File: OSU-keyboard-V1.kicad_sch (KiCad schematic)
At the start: 21 parts, among them J1 AVR-ISP-6, SW1 SW_Push_Dual, U1 ATmega32U4-A, U2 PRTR5V0U2X, Y1 16MHz

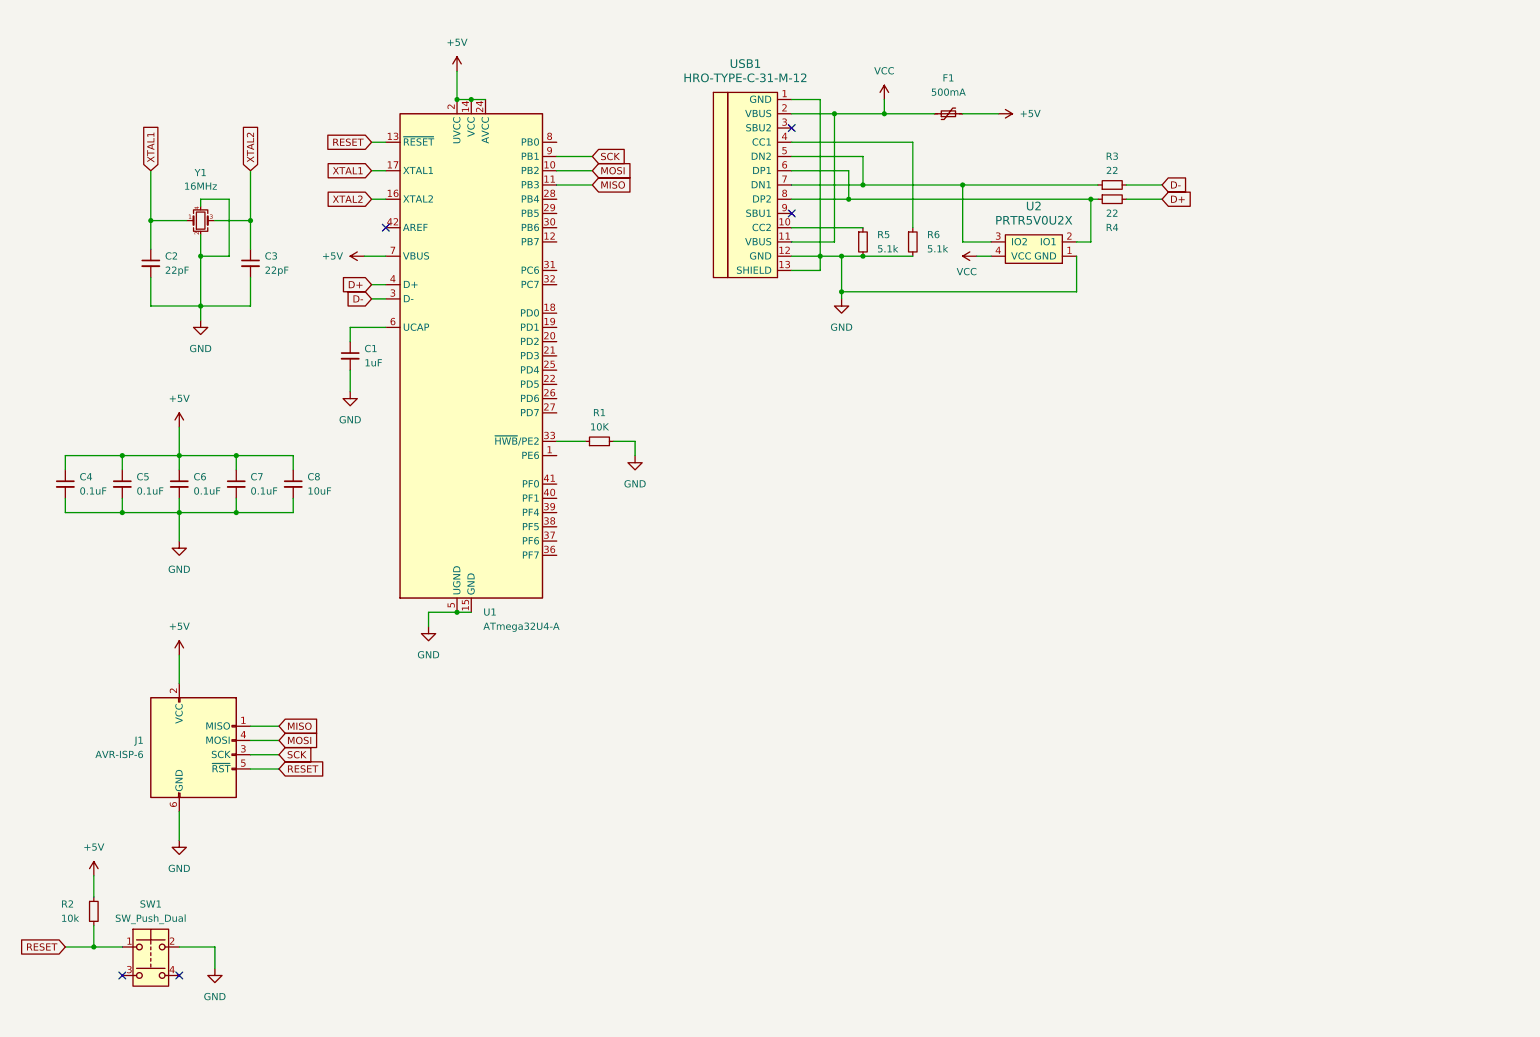
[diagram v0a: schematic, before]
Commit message: Placing components in PCB
Placing all of them (for the first time)
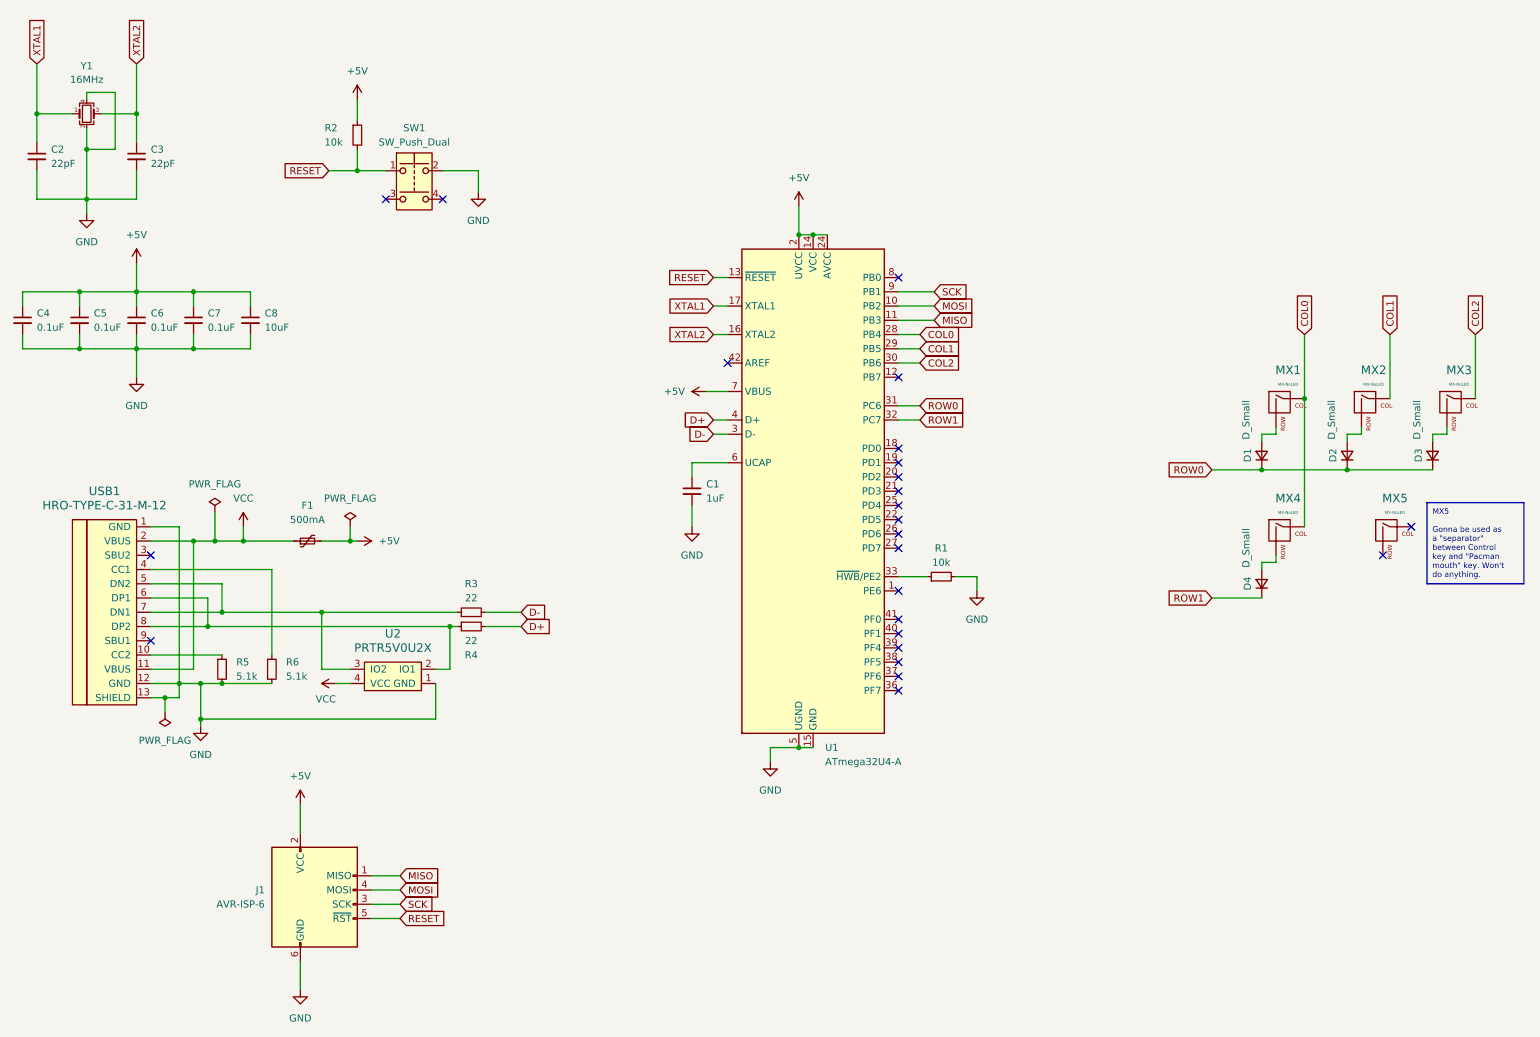
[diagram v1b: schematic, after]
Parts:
- added D1, D2, D3, D4: D_Small, Diode_SMD:D_SOD-123, symbol Device:D_Small
- added MX1, MX2, MX3: MX-NoLED, MX_Alps_Hybrid:MX-1U, symbol MX_Alps_Hybrid:MX-NoLED
- added MX4: MX-NoLED, MX_Alps_Hybrid:MX-1.5U, symbol MX_Alps_Hybrid:MX-NoLED
- added MX5: MX-NoLED, MX_Alps_Hybrid:MX-1.25U, symbol MX_Alps_Hybrid:MX-NoLED
- C1, C2, C3, C4, C5, C6, C7, C8: footprint (none) -> Capacitor_SMD:C_0805_2012Metric_Pad1.18x1.45mm_HandSolder
- F1: footprint (none) -> Fuse:Fuse_1206_3216Metric_Pad1.42x1.75mm_HandSolder
- J1: footprint (none) -> random-keyboard-parts:Reset_Pretty-Mask
- R1: value 10K -> 10k; footprint (none) -> Resistor_SMD:R_0805_2012Metric_Pad1.20x1.40mm_HandSolder
- R2, R3, R4, R5, R6: footprint (none) -> Resistor_SMD:R_0805_2012Metric_Pad1.20x1.40mm_HandSolder
- SW1: footprint (none) -> Button_Switch_SMD:SW_SPST_SKQG_WithStem
- U2: footprint (none) -> random-keyboard-parts:SOT143B
- USB1: footprint (none) -> Type-C:HRO-TYPE-C-31-M-12-HandSoldering
- Y1: footprint (none) -> Crystal:Crystal_SMD_3225-4Pin_3.2x2.5mm_HandSoldering
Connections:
- net COL0: now reaches U1.28 (PB4)
- net COL0: now also MX1.1 (COL), MX4.1 (COL)
- net COL1: now reaches U1.29 (PB5)
- net COL1: now also MX2.1 (COL)
- net COL2: now reaches U1.30 (PB6)
- net COL2: now also MX3.1 (COL)
- net ROW0: now reaches U1.31 (PC6)
- net ROW0: now also D1.1 (K), D2.1 (K), D3.1 (K)
- net ROW1: now reaches U1.32 (PC7)
- net ROW1: now also D4.1 (K)
- new net: D4.2 (A), MX4.2 (ROW)
- new net: D1.2 (A), MX1.2 (ROW)
- new net: D2.2 (A), MX2.2 (ROW)
- new net: D3.2 (A), MX3.2 (ROW)
- no-connect marks 5 -> 24
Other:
- company: (none) -> BitBlitz S.A.C.
- title: (none) -> OSU Keyboard - No Led
- moved on the sheet: C1, C2, C3, C4, C5, C6, C7, C8, F1, J1, R1, R2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
